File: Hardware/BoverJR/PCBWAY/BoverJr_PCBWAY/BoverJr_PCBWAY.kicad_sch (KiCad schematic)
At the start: 50 parts, among them J11 Cable_PAD, J3 Encoder Derecho, J3 Programador, J4 Encoder Izquierdo, J5 Distancia_Der, J6 Cable_PAD, J6 Distancia_Izq, J7 Cable_PAD, J7 Distancia_Frontal, J8 7.4v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

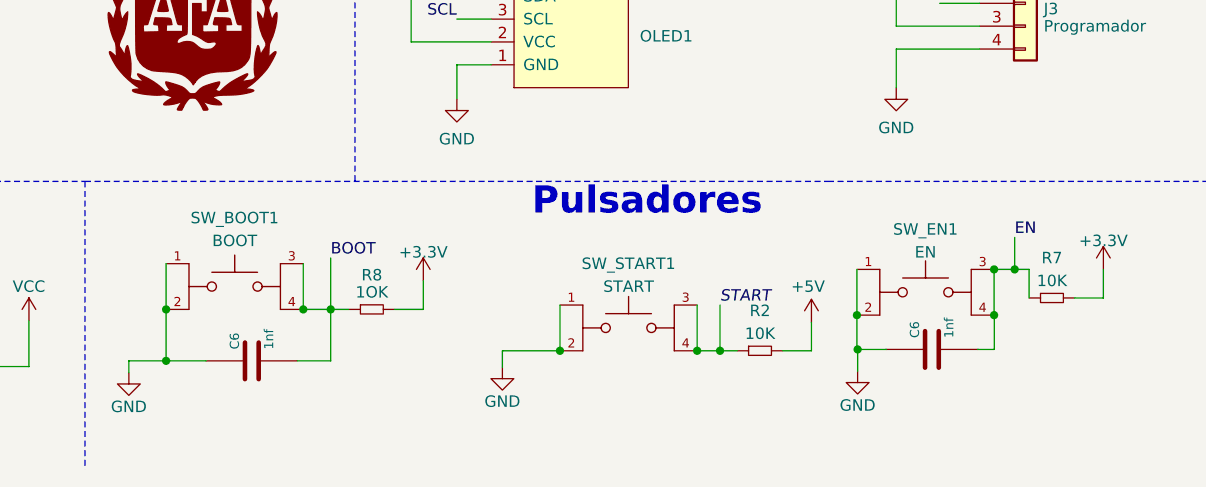
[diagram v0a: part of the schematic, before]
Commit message: AÑADI BOTON A LABERINTO CHASIS PLACA
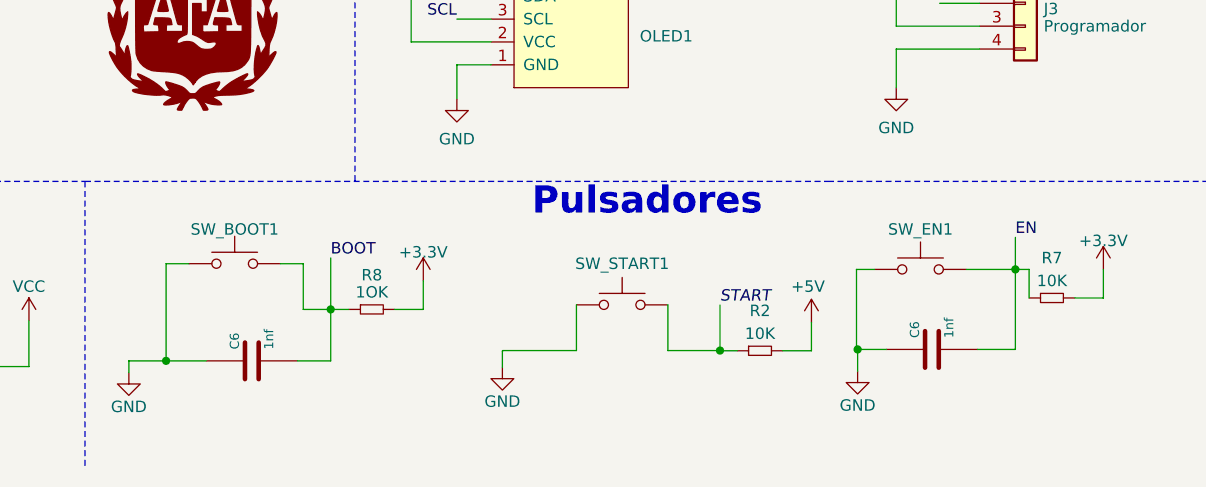
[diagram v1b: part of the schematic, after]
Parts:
- removed SW_BOOT1: BOOT, EESTN5:SW_TL3301FF160QG, symbol switch smd 6mm:TL3301FF160QG
- removed SW_EN1: EN, EESTN5:SW_TL3301FF160QG, symbol switch smd 6mm:TL3301FF160QG
- removed SW_START1: START, EESTN5:SW_TL3301FF160QG, symbol switch smd 6mm:TL3301FF160QG
- added SW_BOOT1, SW_EN1, SW_START1: SW_Push, EESTN5:Pulsador_SMD_2_BAJO, symbol EESTN5:SW_Push
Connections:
- net BOOT: now also SW_BOOT1.2
- net EN: now also SW_EN1.2
- net GND: now also SW_BOOT1.1, SW_EN1.1, SW_START1.1
- net START: now also SW_START1.2

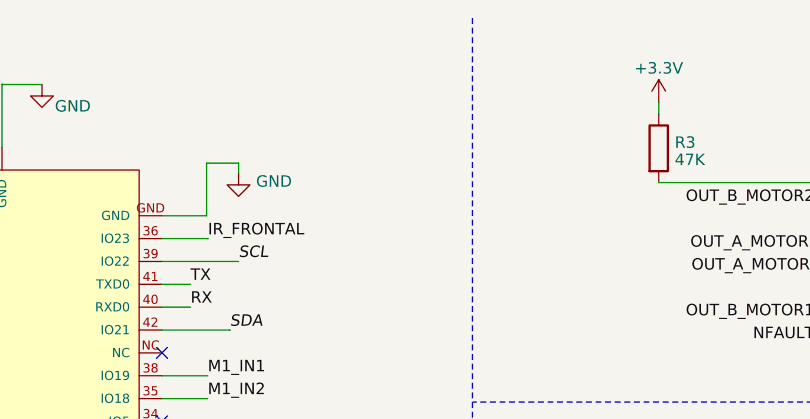
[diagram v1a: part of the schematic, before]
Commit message: corregi pcb bover JR
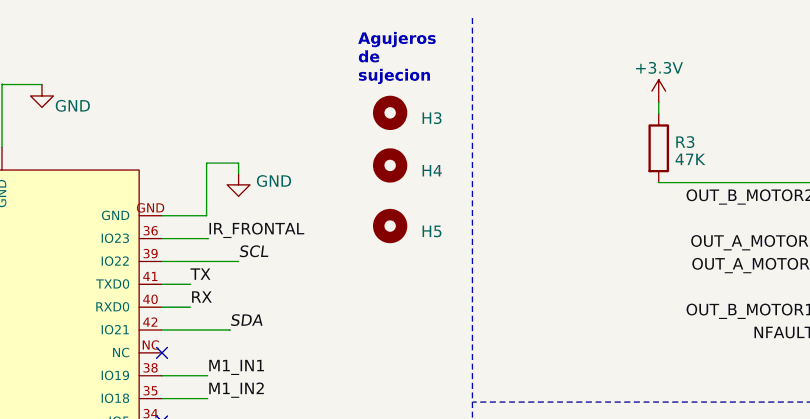
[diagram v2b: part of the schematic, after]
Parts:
- added H3, H4, H5: Mounting_Hole, EESTN5:hole_3mm, symbol EESTN5:Mounting_Hole
- G2: footprint EESTN5:Bover_Huella_frontal_FCU -> EESTN5:Bover_Huella_BCU_SOLK
- G3: footprint EESTN5:AFA -> EESTN5:AFA_BCU_filks
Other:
- note added: "Agujeros de sujecion"
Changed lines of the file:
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@@
     (effects (font (size 3 3) (thickness 0.6) bold) (justify left bottom))
+  )
+  (text "Agujeros \nde \nsujecion" (at 164.211 19.304 0)
+    (effects (font (size 1.27 1.27) (thickness 0.254) bold) (justify left bottom))
   )
   (text "Pulsadores" (at 101.6 170.18 0)
@@
     )
   )
+  (symbol (lib_id "EESTN5:Mounting_Hole") (at 167.767 28.321 0) (unit 1)
+    (in_bom yes) (on_board yes) (dnp no) (fields_autoplaced)
+    (property "Reference" "H4" (at 171.196 28.956 0)
+      (effects (font (size 1.27 1.27)) (justify left))
+    )
+    (property "Value" "Mounting_Hole" (at 167.767 25.146 0)
+      (effects (font (size 1.27 1.27)) hide)
+    )
+    (property "Footprint" "EESTN5:hole_3mm" (at 167.767 28.321 0)
+      (effects (font (size 1.524 1.524)) hide)
+    )
+    (property "Datasheet" "" (at 167.767 28.321 0)
+      (effects (font (size 1.524 1.524)) hide)
+    )
+    (instances
+      (project "BoverJr_PCBWAY"
+        (path "/b7bd9da0-65fe-4d59-8fc7-564649d3d9ed"
+          (reference "H4") (unit 1)
+        )
+      )
+    )
+  )
   (symbol (lib_id "power:GND") (at 98.3234 186.7662 0) (unit 1)
     (in_bom yes) (on_board yes) (dnp no)
@@
     )
   )
+  (symbol (lib_id "EESTN5:Mounting_Hole") (at 167.767 35.052 0) (unit 1)
+    (in_bom yes) (on_board yes) (dnp no) (fields_autoplaced)
+    (property "Reference" "H5" (at 171.196 35.687 0)
+      (effects (font (size 1.27 1.27)) (justify left))
+    )
+    (property "Value" "Mounting_Hole" (at 167.767 31.877 0)
+      (effects (font (size 1.27 1.27)) hide)
+    )
+    (property "Footprint" "EESTN5:hole_3mm" (at 167.767 35.052 0)
+      (effects (font (size 1.524 1.524)) hide)
+    )
+    (property "Datasheet" "" (at 167.767 35.052 0)
+      (effects (font (size 1.524 1.524)) hide)
+    )
+    (instances
+      (project "BoverJr_PCBWAY"
+        (path "/b7bd9da0-65fe-4d59-8fc7-564649d3d9ed"
+          (reference "H5") (unit 1)
+        )
+      )
+    )
+  )
   (symbol (lib_id "Device:C_Small") (at 267.589 36.322 0) (unit 1)
     (in_bom yes) (on_board yes) (dnp no)
@@
       (effects (font (size 1.27 1.27)) hide)
     )
-    (property "Footprint" "EESTN5:AFA" (at 63.9064 143.7132 0)
+    (property "Footprint" "EESTN5:AFA_BCU_filks" (at 63.9064 143.7132 0)
       (effects (font (size 1.27 1.27)) hide)
     )
@@
       (effects (font (size 1.27 1.27)) hide)
     )
-    (property "Footprint" "EESTN5:Bover_Huella_frontal_FCU" (at 29.6418 143.2814 0)
+    (property "Footprint" "EESTN5:Bover_Huella_BCU_SOLK" (at 29.6418 143.2814 0)
       (effects (font (size 1.27 1.27)) hide)
     )
@@
         )
       )
+    )
+  )
+  (symbol (lib_id "EESTN5:Mounting_Hole") (at 167.767 22.479 0) (unit 1)
+    (in_bom yes) (on_board yes) (dnp no) (fields_autoplaced)
+    (property "Reference" "H3" (at 171.196 23.114 0)
+      (effects (font (size 1.27 1.27)) (justify left))
+    )
+    (property "Value" "Mounting_Hole" (at 167.767 19.304 0)
+      (effects (font (size 1.27 1.27)) hide)
+    )
+    (property "Footprint" "EESTN5:hole_3mm" (at 167.767 22.479 0)
+      (effects (font (size 1.524 1.524)) hide)
+    )
+    (property "Datasheet" "" (at 167.767 22.479 0)
+      (effects (font (size 1.524 1.524)) hide)
+    )
+    (instances
+      (project "BoverJr_PCBWAY"
+        (path "/b7bd9da0-65fe-4d59-8fc7-564649d3d9ed"
+          (reference "H3") (unit 1)
+        )
+      )
